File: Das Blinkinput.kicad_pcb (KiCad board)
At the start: 4 copper layers, 50.8 x 25.4 mm, 33 parts, among them P101 CONN_01X02, P102 CONN_01X01, P103 CONN_01X01, P104 CONN_01X01, P105 CONN_01X05, P201 CONN_01X01, P301 CONN_01X01, P401 CONN_01X01, P501 CONN_01X01, U101 LP2980IM5-3.0/NOPB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

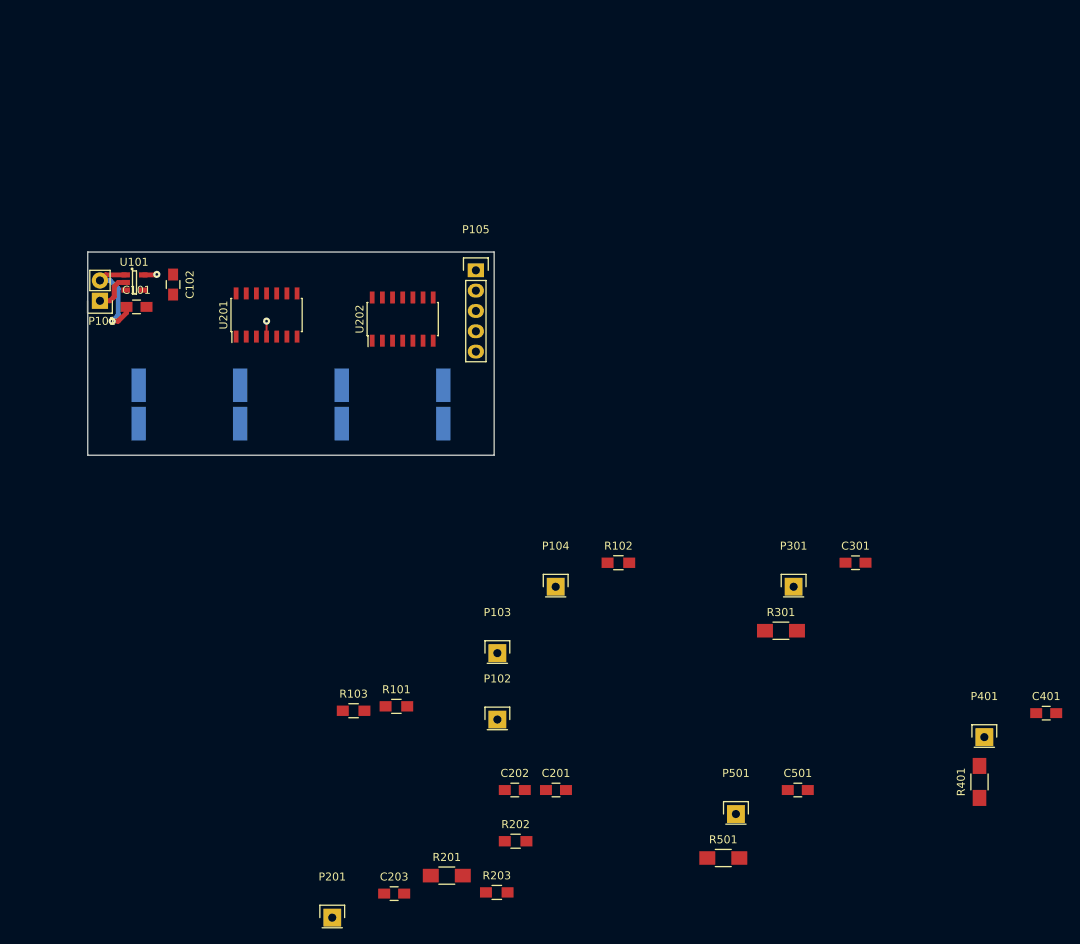
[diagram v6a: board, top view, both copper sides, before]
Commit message: Did power layout and began op amp connection
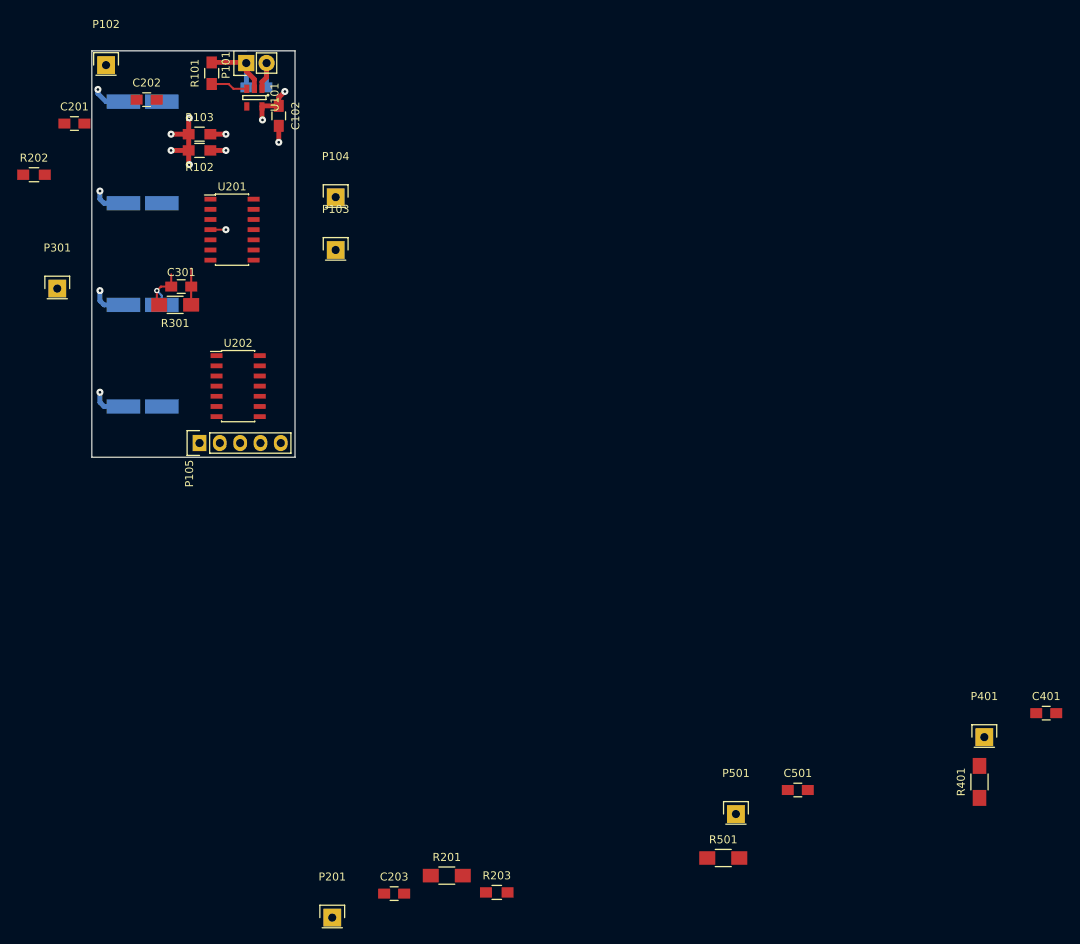
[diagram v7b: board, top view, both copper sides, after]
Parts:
- C101: moved to B.Cu
- moved R202 102.8 mm to (70.8, 83.0)
- moved C201 102.8 mm to (75.8, 76.6)
- moved P301 99.3 mm to (73.7, 97.3)
- moved C202 97.8 mm to (84.8, 73.7)
- moved P102 95.3 mm to (79.8, 69.3)
- moved C301 91.1 mm to (89.2, 97.0), turned to 180 degrees
- moved R301 86.0 mm to (88.4, 99.3), turned to 180 degrees
- moved R101 82.4 mm to (93.0, 70.4), turned to 90 degrees
- moved R103 74.6 mm to (91.4, 78.0)
- moved R102 73.5 mm to (91.4, 80.0), turned to 180 degrees
- moved P104 55.9 mm to (108.5, 85.9)
- moved P103 54.3 mm to (108.5, 92.5)
- moved P105 40.7 mm to (91.4, 116.6), turned to 90 degrees
- moved PD201 37.8 mm to (84.3, 73.9), turned to 0 degrees
- moved PD401 37.6 mm to (84.3, 112.0), turned to 0 degrees
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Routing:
- net VGND: track 0.00 -> 27.4 mm, vias 0 -> 8
- net GND: track 4.91 -> 15.1 mm, vias 0 -> 2
- net Net-(C301-Pad2): track 0.00 -> 7.48 mm, vias 0 -> 1
- net Net-(C101-Pad1): track 13.6 -> 6.51 mm, vias 1 -> 0
- net 3V: track 3.66 -> 9.85 mm, vias 2 -> 4
- net Net-(R101-Pad1): track 0.00 -> 5.48 mm
- net Net-(C301-Pad1): track 0.00 -> 4.56 mm
- added copper zone on GND.Cu, net VGND
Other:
- board size 50.8 x 25.4 mm -> 25.4 x 50.8 mm
- net class Default: clearance 0.1524 -> 0.254; trace_width 0.1524 -> 0.254
- rule trace_clearance: 0.1524 -> 0.254

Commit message: Routed all passives related to U201 and the photodiodes
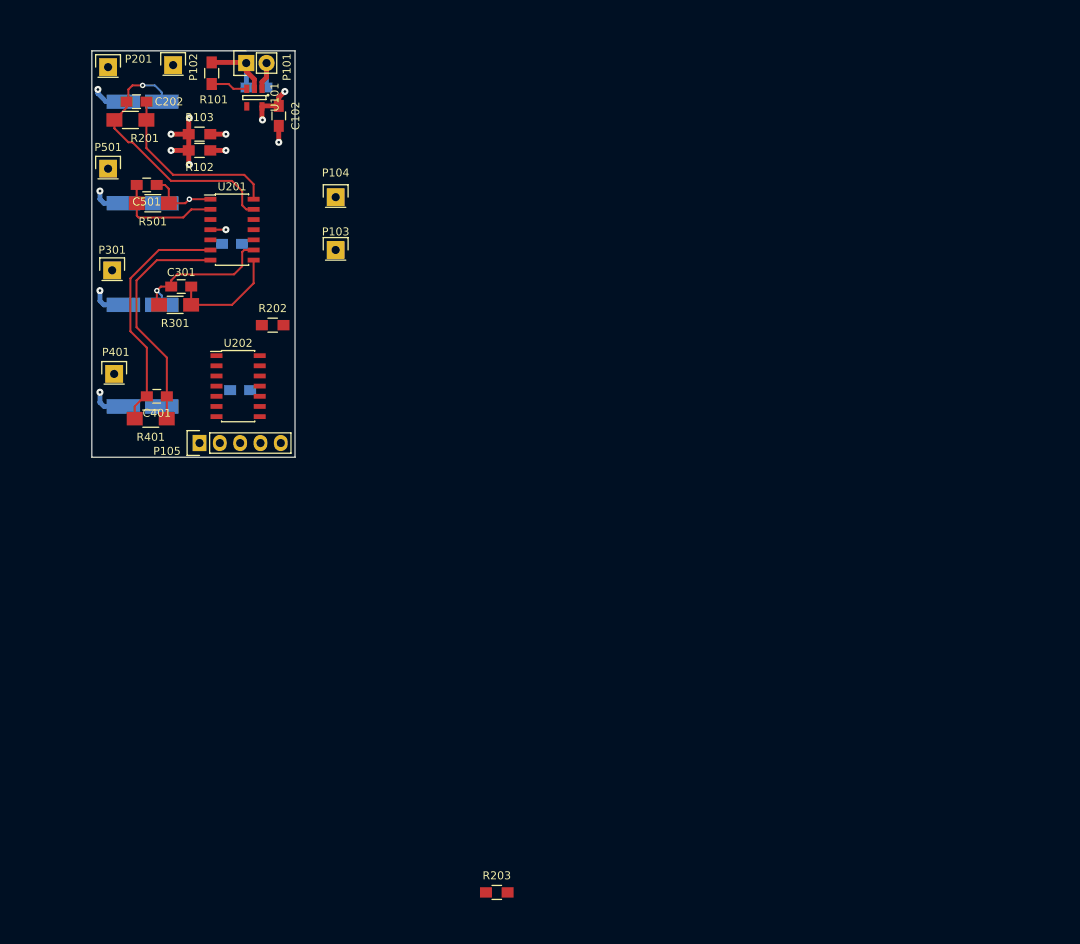
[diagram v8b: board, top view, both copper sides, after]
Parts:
- C201, C203: moved to B.Cu
- moved C401 118.0 mm to (86.1, 110.7), turned to 180 degrees
- moved P401 117.9 mm to (80.8, 108.0)
- moved R401 113.1 mm to (85.3, 113.5), turned to 180 degrees
- moved P501 112.5 mm to (80.0, 82.3)
- moved C501 111.1 mm to (84.8, 84.3), turned to 180 degrees
- moved P201 109.9 mm to (80.0, 69.6)
- moved R501 108.6 mm to (85.6, 86.6), turned to 180 degrees
- moved R201 102.4 mm to (82.8, 76.2), turned to 180 degrees
- moved C203 65.8 mm to (96.5, 110.0), turned to 180 degrees
- moved R202 35.3 mm to (100.6, 101.9)
- moved C201 24.8 mm to (95.5, 91.7), turned to 180 degrees
- moved P102 8.38 mm to (88.1, 69.3)
- moved P301 7.23 mm to (80.5, 95.0)
- moved C202 1.30 mm to (83.6, 73.9), turned to 180 degrees
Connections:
- U201 pad 1: Net-(C202-Pad1) -> Net-(C501-Pad1)
- U201 pad 13: Net-(C501-Pad2) -> Net-(C202-Pad2)
- U201 pad 14: Net-(C501-Pad1) -> Net-(C202-Pad1)
- U201 pad 2: Net-(C202-Pad2) -> Net-(C501-Pad2)
- U201 pad 6: Net-(C301-Pad2) -> Net-(C401-Pad2)
- U201 pad 7: Net-(C301-Pad1) -> Net-(C401-Pad1)
- U201 pad 8: Net-(C401-Pad1) -> Net-(C301-Pad1)
- U201 pad 9: Net-(C401-Pad2) -> Net-(C301-Pad2)
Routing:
- net Net-(C202-Pad2): track 0.00 -> 34.1 mm, vias 0 -> 1
- net Net-(C401-Pad2): track 0.00 -> 30.6 mm
- net Net-(C401-Pad1): track 0.00 -> 29.1 mm
- net Net-(C202-Pad1): track 0.00 -> 23.0 mm
- net Net-(C501-Pad2): track 0.00 -> 13.6 mm
- net Net-(C301-Pad2): track 7.48 -> 19.6 mm
- net Net-(C301-Pad1): track 4.56 -> 14.1 mm
- net Net-(C501-Pad1): track 0.00 -> 8.94 mm, vias 0 -> 1
